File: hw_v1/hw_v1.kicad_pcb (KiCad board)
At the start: 4 copper layers, 116.5 x 98 mm, 230 parts, among them J10 Conn_01x01, J11 Conn_01x01, J12 Delphi_Sicma_24, J13 Delphi_Sicma_24, J14 Conn_01x04, J2 Conn_01x05, J3 Conn_01x05, J4 Conn_01x05, J5 Conn_01x03, J6 Conn_01x04, J8 USB_B, J9 Tag connect, Q1 AO3400A, Q2 AO3400A, Q3 FDS6890A, Q5 SS8050, Q6 AO3400A, SW2 SW_Push, U1 MCZ33810EK, U10 BMP280, U11 L78M05ABDT-TR, U12 LM74800, U13 STM32F407VGTx, U14 TJA1051T-3, U15 25LCxxx, U16 REF3033, U17 SRV05-4, U18 VNLD5090, U19 L78M05ABDT-TR, U2 TC4424A, U21 ADXL343, U3 TC4424A, U4 MAX9926UAEE+, U5 TPL7407LAPWR, U6 LMV324, U7 LMV324, U9 SP720ABTG, Y1 32.768kHz, Y2 25MHz

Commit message: wip sensors pcb layout
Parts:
- added C1: 100nF, Capacitor_SMD:C_0805_2012Metric, F.Cu at (109.5, 73.6)
- added C25: 100nF, Capacitor_SMD:C_0805_2012Metric, F.Cu at (89.5, 73.5)
- added C29: 0.22uF, Capacitor_SMD:C_0603_1608Metric, F.Cu at (91.7, 70.2)
- added C30: 100nF, Capacitor_SMD:C_0805_2012Metric, F.Cu at (76.4, 73.5)
- added C31: 0.01uF, Capacitor_SMD:C_0805_2012Metric, F.Cu at (116.0, 73.4)
- added C46: 0.22uF, Capacitor_SMD:C_0603_1608Metric, F.Cu at (80.3, 73.4)
- added C49: 0.22uF, Capacitor_SMD:C_0603_1608Metric, F.Cu at (113.3, 73.3)
- added C66: 100nF, Capacitor_SMD:C_0805_2012Metric, F.Cu at (83.0, 73.5)
- added C67: 0.22uF, Capacitor_SMD:C_0603_1608Metric, F.Cu at (86.9, 73.4)
- added C68: 100nF, Capacitor_SMD:C_0805_2012Metric, F.Cu at (102.9, 73.7)
- added C69: 0.22uF, Capacitor_SMD:C_0603_1608Metric, F.Cu at (106.7, 73.5)
- added C70: 100nF, Capacitor_SMD:C_0805_2012Metric, F.Cu at (96.3, 73.7)
- added C71: 0.22uF, Capacitor_SMD:C_0603_1608Metric, F.Cu at (100.1, 73.5)
- added Q14: AO3400A, Package_TO_SOT_SMD:SOT-23, F.Cu at (97.4, 82.5)
- added Q15: AO3400A, Package_TO_SOT_SMD:SOT-23, F.Cu at (100.8, 86.4)
- added Q16: AO3400A, Package_TO_SOT_SMD:SOT-23, F.Cu at (93.9, 78.6)
- added Q19: AO3400A, Package_TO_SOT_SMD:SOT-23, F.Cu at (118.9, 73.3)
- added R10: 180k, Resistor_SMD:R_0805_2012Metric, F.Cu at (84.2, 90.2)
- added R13: 180k, Resistor_SMD:R_0805_2012Metric, F.Cu at (78.2, 90.2)
- added R16: 604R, Resistor_SMD:R_0805_2012Metric, F.Cu at (91.6, 73.5)
- added R18: 10k, Resistor_SMD:R_0805_2012Metric, F.Cu at (93.9, 83.4)
- added R28: 3.88k, Resistor_SMD:R_0603_1608Metric, F.Cu at (93.4, 70.2)
- added R44: 348k, Resistor_SMD:R_0805_2012Metric, F.Cu at (78.2, 93.7)
- added R45: 470R, Resistor_SMD:R_0603_1608Metric, F.Cu at (105.9, 71.3)
- added R46: 2.49k +-1%, Resistor_SMD:R_0603_1608Metric, F.Cu at (105.2, 73.5)
- added R47: 180k, Resistor_SMD:R_0805_2012Metric, F.Cu at (76.2, 90.2)
- added R48: 348k, Resistor_SMD:R_0805_2012Metric, F.Cu at (76.2, 93.7)
- added R49: 10k, Resistor_SMD:R_0805_2012Metric, F.Cu at (93.9, 81.3)
- added R50: 10k, Resistor_SMD:R_0805_2012Metric, F.Cu at (93.9, 85.4)
- added R51: 10k, Resistor_SMD:R_0805_2012Metric, F.Cu at (97.8, 79.2)
- added R52: 10k, Resistor_SMD:R_0805_2012Metric, F.Cu at (93.9, 87.4)
- added R53: 10k, Resistor_SMD:R_0805_2012Metric, F.Cu at (97.4, 85.4)
- added R54: 2.49k +-1%, Resistor_SMD:R_0603_1608Metric, F.Cu at (85.3, 73.4)
- added R55: 180k, Resistor_SMD:R_0805_2012Metric, F.Cu at (80.2, 90.2)
- added R56: 470R, Resistor_SMD:R_0603_1608Metric, F.Cu at (93.5, 73.5)
- added R57: 180k, Resistor_SMD:R_0805_2012Metric, F.Cu at (86.2, 90.2)
- added R61: 348k, Resistor_SMD:R_0805_2012Metric, F.Cu at (80.2, 93.7)
- added R62: 180k, Resistor_SMD:R_0805_2012Metric, F.Cu at (88.2, 90.2)
- added R63: 348k, Resistor_SMD:R_0805_2012Metric, F.Cu at (88.2, 93.7)
- added R66: 348k, Resistor_SMD:R_0805_2012Metric, F.Cu at (86.2, 93.7)
- added R67: 180k, Resistor_SMD:R_0805_2012Metric, F.Cu at (82.1, 90.2)
- added R69: 348k, Resistor_SMD:R_0805_2012Metric, F.Cu at (82.1, 93.7)
- added R7: 348k, Resistor_SMD:R_0805_2012Metric, F.Cu at (84.2, 93.7)
- added R74: 2.49k +-1%, Resistor_SMD:R_0603_1608Metric, F.Cu at (78.7, 73.4)
- added R75: 470R, Resistor_SMD:R_0603_1608Metric, F.Cu at (86.1, 71.1)
- added R76: 470R, Resistor_SMD:R_0603_1608Metric, F.Cu at (99.3, 71.3)
- added R77: 470R, Resistor_SMD:R_0603_1608Metric, F.Cu at (79.5, 71.2)
- added R78: 470R, Resistor_SMD:R_0603_1608Metric, F.Cu at (112.6, 70.9)
- added R85: 1k, Resistor_SMD:R_0603_1608Metric, F.Cu at (119.2, 70.5)
- added TP14: TestPoint_Alt, TestPoint:TestPoint_THTPad_1.0x1.0mm_Drill0.5mm, F.Cu at (83.0, 70.7)
- added TP15: TestPoint_Alt, TestPoint:TestPoint_THTPad_1.0x1.0mm_Drill0.5mm, F.Cu at (102.8, 70.9)
- added TP19: TestPoint_Alt, TestPoint:TestPoint_THTPad_1.0x1.0mm_Drill0.5mm, F.Cu at (96.3, 70.9)
- added TP20: TestPoint_Alt, TestPoint:TestPoint_THTPad_1.0x1.0mm_Drill0.5mm, F.Cu at (89.7, 70.6)
- added TP23: TestPoint_Alt, TestPoint:TestPoint_THTPad_1.0x1.0mm_Drill0.5mm, F.Cu at (76.4, 70.7)
- added TP25: TestPoint_Alt, TestPoint:TestPoint_THTPad_1.0x1.0mm_Drill0.5mm, F.Cu at (109.5, 70.6)
- added TP38: TestPoint_Alt, TestPoint:TestPoint_THTPad_1.0x1.0mm_Drill0.5mm, F.Cu at (116.0, 70.6)
- added U10: LMV324, Package_SO:TSSOP-14_4.4x5mm_P0.65mm, F.Cu at (103.1, 91.9)
- added U2: 74HC4851, Package_SO:SOIC-16_3.9x9.9mm_P1.27mm, F.Cu at (88.0, 83.2)
- added U26: SP720ABTG, Package_SO:SOP-16_3.9x9.9mm_P1.27mm, F.Cu at (79.0, 83.2)
- added U9: LMV324, Package_SO:TSSOP-14_4.4x5mm_P0.65mm, F.Cu at (94.2, 91.9)
- moved D3 194.3 mm to (64.4, 110.6), turned to 90 degrees
- moved D6 192.0 mm to (66.5, 110.6), turned to 90 degrees
- moved TP15 189.8 mm to (22.1, 51.0), turned to 90 degrees
- moved D8 189.7 mm to (68.6, 110.6), turned to 90 degrees
- moved TP16 188.1 mm to (25.1, 51.0), turned to 90 degrees
- moved D11 187.4 mm to (70.7, 110.6), turned to 90 degrees
- moved TP11 185.9 mm to (22.1, 54.0), turned to 90 degrees
- moved TP14 184.1 mm to (25.1, 54.0), turned to 90 degrees
- moved TP9 182.0 mm to (22.1, 57.1), turned to 90 degrees
- moved RN1 181.5 mm to (67.5, 101.2), turned to -90 degrees
- moved D12 180.9 mm to (64.4, 97.4), turned to -90 degrees
- moved D2 180.7 mm to (64.3, 106.7), turned to 90 degrees
- moved TP10 180.2 mm to (25.1, 57.1), turned to 90 degrees
- moved RN2 179.1 mm to (74.0, 106.6), turned to -90 degrees
- moved D9 178.3 mm to (66.5, 97.4), turned to -90 degrees
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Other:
- board text added: "1"
- board text added: "ACC"
- board text added: "Analog frontend"
- board text added: "CLT"
- board text added: "EXT O2"
- board text added: "IAT"
- board text added: "Ignicion"
- board text added: "Inyeccion"
- board text added: "MAP"
- board text added: "TPS"
- board text added: "VBAT"

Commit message: wip sensors pcb layout
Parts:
- removed the C1 at (200.2, 55.3)
- removed the C1 at (109.5, 73.6)
- removed the C25 at (234.9, 137.5)
- removed the C25 at (89.5, 73.5)
- removed the C29 at (91.7, 70.2)
- removed the C29 at (173.3, 58.3)
- removed the C30 at (173.3, 61.3)
- removed the C30 at (76.4, 73.5)
- removed the C31 at (173.3, 64.3)
- removed the C31 at (116.0, 73.4)
- removed the C46 at (80.3, 73.4)
- removed the C46 at (188.3, 95.8)
- removed the C49 at (113.3, 73.3)
- removed C66, C68, C70: 100nF, Capacitor_SMD:C_0805_2012Metric
- removed C67, C69, C71: 0.22uF, Capacitor_SMD:C_0603_1608Metric
- removed Q14, Q15, Q16, Q19: AO3400A, Package_TO_SOT_SMD:SOT-23
- removed the R10 at (84.2, 90.2)
- removed the R10 at (215.0, 75.1)
- removed the R13 at (78.2, 90.2)
- removed the R13 at (234.9, 122.1)
- removed the R16 at (234.9, 125.1)
- removed the R16 at (91.6, 73.5)
- removed the R18 at (33.0, 65.8)
- removed the R18 at (93.9, 83.4)
- removed the R28 at (30.5, 61.8)
- removed the R28 at (93.4, 70.2)
- removed the R44 at (180.8, 100.2)
- removed the R44 at (78.2, 93.7)
- removed the R45 at (31.8, 98.8)
- removed the R45 at (105.9, 71.3)
- removed the R46 at (17.1, 94.4)
- removed the R46 at (105.2, 73.5)
- removed the R47 at (76.2, 90.2)
- removed the R47 at (20.0, 94.4)
- removed the R48 at (76.2, 93.7)
- removed the R48 at (228.2, 101.4)
- removed the R49 at (93.9, 81.3)
- removed the R49 at (228.2, 103.9)
- removed the R50 at (22.9, 94.4)
- removed the R50 at (93.9, 85.4)
- removed the R51 at (25.9, 94.4)
- removed the R51 at (97.8, 79.2)
- removed the R52 at (28.9, 94.4)
- removed the R52 at (93.9, 87.4)
- removed the R53 at (97.4, 85.4)
- removed the R53 at (246.6, 134.5)
- removed the R54 at (246.6, 137.0)
- removed the R54 at (85.3, 73.4)
- removed the R55 at (80.2, 90.2)
- removed the R55 at (251.7, 125.8)
- removed the R56 at (93.5, 73.5)
- removed the R56 at (251.7, 128.7)
- removed the R57 at (251.7, 131.7)
- removed the R57 at (86.2, 90.2)
- removed the R61 at (228.2, 111.4)
- removed the R61 at (80.2, 93.7)
- removed the R62 at (88.2, 90.2)
- removed the R63 at (88.2, 93.7)
- removed the R66 at (86.2, 93.7)
- removed the R67 at (82.1, 90.2)
- removed R69: 348k, Resistor_SMD:R_0805_2012Metric
- removed the R7 at (84.2, 93.7)
- removed the R7 at (195.2, 72.7)
- removed R74: 2.49k +-1%, Resistor_SMD:R_0603_1608Metric
- removed R75, R76, R77, R78: 470R, Resistor_SMD:R_0603_1608Metric
- removed R85: 1k, Resistor_SMD:R_0603_1608Metric
- removed the TP14 at (25.1, 54.0)
- removed the TP14 at (83.0, 70.7)
- removed the TP15 at (22.1, 51.0)
- removed the TP15 at (102.8, 70.9)
- removed TP19, TP20, TP23, TP25, TP38: TestPoint_Alt, TestPoint:TestPoint_THTPad_1.0x1.0mm_Drill0.5mm
- removed the U10 at (125.7, 102.5)
- removed the U10 at (103.1, 91.9)
- removed the U2 at (88.0, 83.2)
- removed U26: SP720ABTG, Package_SO:SOP-16_3.9x9.9mm_P1.27mm
- removed the U9 at (94.2, 91.9)
- removed the U9 at (22.3, 86.5)
- added C1: 0.01uF, Capacitor_SMD:C_0805_2012Metric, F.Cu at (222.3, 60.6)
- added C25: 0.1uF, Capacitor_SMD:C_0805_2012Metric, F.Cu at (240.4, 110.0)
- added C29: 2.2uF, Capacitor_SMD:C_0805_2012Metric, F.Cu at (192.0, 63.7)
- added C30: 100nF, Capacitor_SMD:C_0805_2012Metric, F.Cu at (192.0, 66.7)
- added C31: 100nF, Capacitor_SMD:C_0805_2012Metric, F.Cu at (192.0, 69.7)
- added C46: 100n, Capacitor_SMD:C_0402_1005Metric, F.Cu at (207.9, 76.1)
- added R10: 10k, Resistor_SMD:R_0603_1608Metric, F.Cu at (226.6, 79.6)
- added R13: 470R, Resistor_SMD:R_0805_2012Metric, F.Cu at (102.1, 70.6)
- added R16: 1k, Resistor_SMD:R_0805_2012Metric, F.Cu at (240.3, 97.6)
- added R18: 470R, Resistor_SMD:R_0603_1608Metric, F.Cu at (95.6, 71.1)
- added R28: 470R, Resistor_SMD:R_0603_1608Metric, F.Cu at (95.6, 78.9)
- added R44: 4.7k, Resistor_SMD:R_0603_1608Metric, F.Cu at (187.8, 78.0)
- added R45: 180k, Resistor_SMD:R_0805_2012Metric, F.Cu at (192.4, 97.6)
- added R46: 180k, Resistor_SMD:R_0805_2012Metric, F.Cu at (191.6, 100.4)
- added R47: 180k, Resistor_SMD:R_0805_2012Metric, F.Cu at (196.8, 91.7)
- added R48: 1k, Resistor_SMD:R_0603_1608Metric, F.Cu at (211.1, 117.8)
- added R49: 1k, Resistor_SMD:R_0603_1608Metric, F.Cu at (211.1, 120.3)
- added R50: 348k, Resistor_SMD:R_0805_2012Metric, F.Cu at (196.8, 94.7)
- added R51: 348k, Resistor_SMD:R_0805_2012Metric, F.Cu at (196.8, 97.6)
- added R52: 348k, Resistor_SMD:R_0805_2012Metric, F.Cu at (196.8, 100.6)
- added R53: 1k, Resistor_SMD:R_0603_1608Metric, F.Cu at (227.0, 130.9)
- added R54: 100k, Resistor_SMD:R_0603_1608Metric, F.Cu at (227.0, 133.4)
- added R55: 100k, Resistor_SMD:R_0805_2012Metric, F.Cu at (232.1, 122.2)
- added R56: 100k, Resistor_SMD:R_0805_2012Metric, F.Cu at (232.1, 125.2)
- added R57: 1k, Resistor_SMD:R_0805_2012Metric, F.Cu at (232.1, 128.2)
- added R61: 1k, Resistor_SMD:R_0603_1608Metric, F.Cu at (211.1, 127.8)
- added R7: 4.99K 1/2W, Resistor_SMD:R_1210_3225Metric, F.Cu at (217.3, 78.1)
- added TP14: TestPoint_Alt, TestPoint:TestPoint_THTPad_1.0x1.0mm_Drill0.5mm, F.Cu at (79.3, 78.5)
- added TP15: TestPoint_Alt, TestPoint:TestPoint_THTPad_1.0x1.0mm_Drill0.5mm, F.Cu at (86.0, 78.5)
- added TP17: TestPoint_Alt, TestPoint:TestPoint_THTPad_1.0x1.0mm_Drill0.5mm, F.Cu at (99.2, 78.6)
- added TP18: TestPoint_Alt, TestPoint:TestPoint_THTPad_1.0x1.0mm_Drill0.5mm, F.Cu at (99.2, 70.6)
- added U10: BMP280, Package_LGA:Bosch_LGA-8_2x2.5mm_P0.65mm_ClockwisePinNumbering, F.Cu at (200.7, 103.9)
- added U9: SP720ABTG, Package_SO:SOP-16_3.9x9.9mm_P1.27mm, F.Cu at (194.4, 107.8)
- moved R35 171.0 mm to (188.0, 94.7), turned to 0 degrees
- moved R36 168.0 mm to (188.0, 97.6), turned to 0 degrees
- moved R17 166.9 mm to (183.5, 91.7), turned to 0 degrees
- moved R40 166.6 mm to (192.4, 91.7), turned to 0 degrees
- moved R39 165.0 mm to (188.0, 100.6), turned to 0 degrees
- moved R23 160.8 mm to (183.5, 94.7), turned to 0 degrees
- moved R24 157.7 mm to (183.5, 97.6), turned to 0 degrees
- moved R33 156.6 mm to (188.0, 91.7), turned to 0 degrees
- moved R26 154.7 mm to (183.5, 100.6), turned to 0 degrees
- moved U6 150.0 mm to (185.7, 105.3), turned to 0 degrees
- moved C20 148.8 mm to (99.2, 73.5), turned to -90 degrees
- moved R41 147.4 mm to (176.0, 90.8), turned to 0 degrees
- moved C19 144.6 mm to (99.2, 81.5), turned to -90 degrees
- moved U7 144.4 mm to (185.7, 111.9), turned to 0 degrees
- moved R12 138.8 mm to (102.1, 78.6), turned to 180 degrees
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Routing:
- net /Sensors/CH_VBATT_m: track 0.00 -> 9.14 mm, vias 0 -> 1
- net Net-(C23-Pad1): track 0.00 -> 6.29 mm
- net /Sensors/CH_O2_m: track 0.00 -> 6.07 mm
- net /Sensors/CH_MAP_m: track 0.00 -> 5.92 mm
- net /Protoboard/ext_a0_in: track 0.00 -> 5.91 mm
- net /Sensors/CH_TPS_m: track 0.00 -> 5.89 mm
- net /Sensors/CH_CLT_m: track 0.00 -> 5.89 mm
- net /Sensors/CH_IAT_m: track 0.00 -> 5.86 mm
- net /Protoboard/ext_a1_in: track 0.00 -> 5.80 mm
- net O2_Sensor: track 0.00 -> 5.69 mm
- net TPS_Sensor: track 0.00 -> 5.32 mm
- net CH_MAP: track 0.00 -> 4.63 mm
- net IAT_Sensor: track 0.00 -> 4.62 mm
- net CLT_Sensor: track 0.00 -> 4.56 mm
- net Net-(D5-K): track 0.00 -> 3.72 mm
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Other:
- board text added: "AUX_IN0"
- board text added: "AUX_IN1"
- board text added: "Inyección"
- board text removed: "ACC"
- board text removed: "Analog frontend"
- board text removed: "Inyeccion"

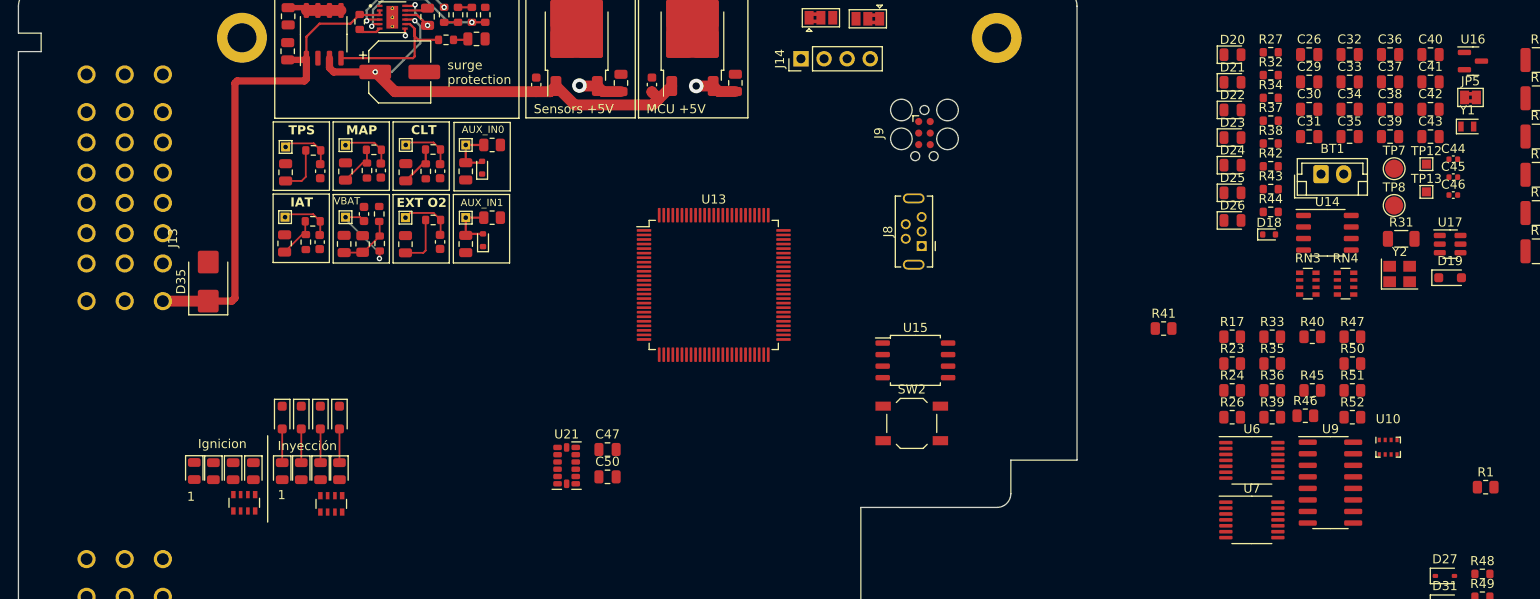
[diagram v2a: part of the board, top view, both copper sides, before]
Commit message: wip sensors traces, added can
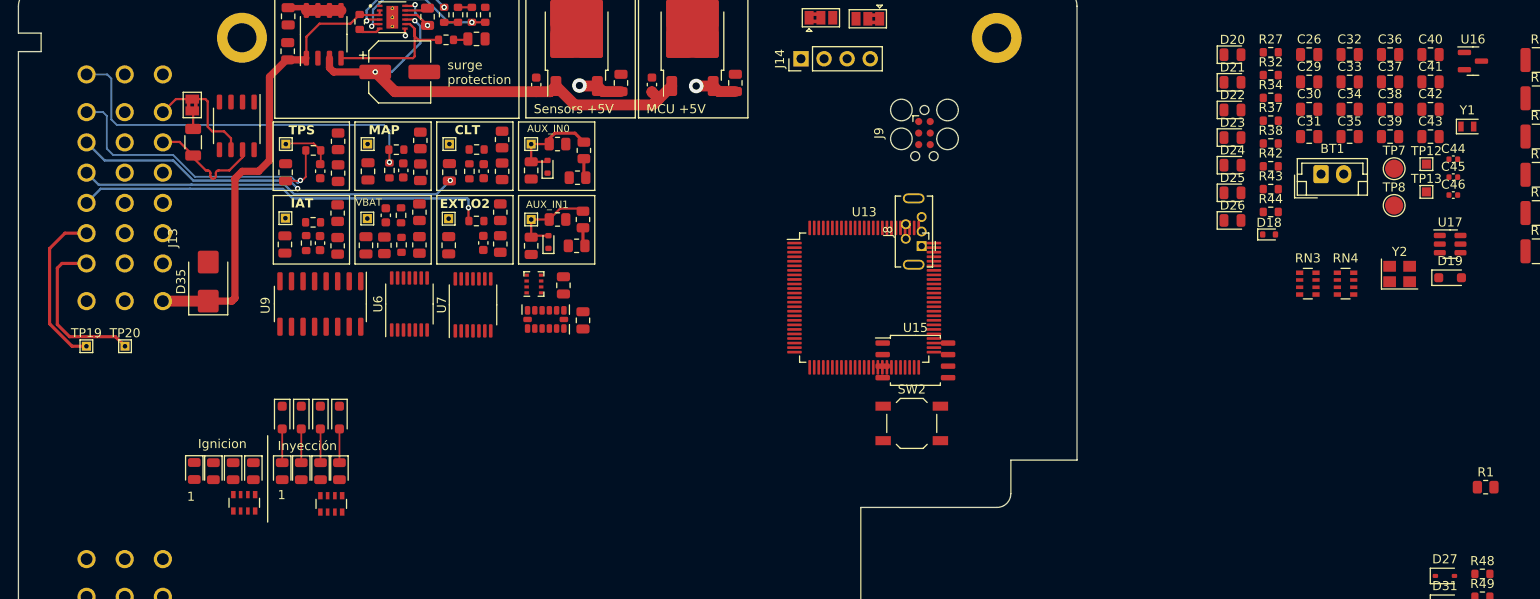
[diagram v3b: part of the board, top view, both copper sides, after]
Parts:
- added TP19: TestPoint_Alt, TestPoint:TestPoint_THTPad_1.0x1.0mm_Drill0.5mm, F.Cu at (57.5, 92.8)
- added TP20: TestPoint_Alt, TestPoint:TestPoint_THTPad_1.0x1.0mm_Drill0.5mm, F.Cu at (61.7, 92.8)
- moved JP5 140.7 mm to (69.1, 66.2), turned to -90 degrees
- moved R31 133.4 mm to (69.2, 70.3), turned to -90 degrees
- moved U14 120.6 mm to (74.0, 68.5), turned to -90 degrees
- moved R51 114.9 mm to (85.2, 70.2), turned to 90 degrees
- moved U9 112.9 mm to (83.2, 88.1), turned to -90 degrees
- moved R46 109.7 mm to (85.2, 73.7), turned to -90 degrees
- moved R39 105.3 mm to (85.1, 78.1), turned to 90 degrees
- moved R33 103.3 mm to (85.1, 81.7), turned to 90 degrees
- moved R40 99.2 mm to (94.1, 78.0), turned to 90 degrees
- moved R36 96.8 mm to (94.2, 73.6), turned to -90 degrees
- moved R50 96.8 mm to (103.2, 70.0), turned to 90 degrees
- moved R52 96.5 mm to (103.0, 78.0), turned to 90 degrees
- moved U10 95.7 mm to (106.7, 85.9), turned to 90 degrees
- moved R35 94.8 mm to (94.1, 81.6), turned to -90 degrees
- moved R47 94.3 mm to (103.0, 81.5), turned to -90 degrees
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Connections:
- net CAM-IN+ renamed CRANK-
- net CRANK-IN+ renamed CAM-
- net CRANK-IN- renamed CRANK+
- net IGN1 renamed STEPPER-B2
- net IGN2 renamed STEPPER-B1
- net IGN4 renamed STEPPER-A2
- C13 pad 1: CH_MAP -> MAP_Sensor
- C19 pad 1: /Protoboard/ext_a0_in -> ext_a0_in
- C20 pad 1: /Protoboard/ext_a1_in -> ext_a1_in
- D16 pad 2: /Protoboard/ext_a0_in -> ext_a0_in
- D17 pad 2: /Protoboard/ext_a1_in -> ext_a1_in
- J12 pad A1: INJ1 -> INJ-1-OUT
- J12 pad A2: INJ2 -> INJ-2-OUT
- J12 pad A3: INJ3 -> INJ-3-OUT
- J12 pad A4: INJ4 -> INJ-4-OUT
- J12 pad A5: INJ5 -> IGN-1-OUT
- J12 pad A6: INJ6 -> IGN-2-OUT
- J12 pad A7: INJ7 -> IGN-3-OUT
- J12 pad A8: INJ8 -> IGN-4-OUT
- J12 pad B3: IGN3 -> STEPPER-A1
- J12 pad B5: IGN5 -> FAN-OUT
- J12 pad B6: IGN6 -> FAN2-OUT
- J12 pad B7: IGN7 -> FUELPUMP-OUT
- J12 pad B8: IGN8 -> TACHO-OUT
- J12 pad C2: FAN-OUT -> VVT-OUT
- J12 pad C3: SPARE2-OUT -> IDLE-OUT
- J12 pad C4: IDLE-OUT -> PROTO-4
- J12 pad C5: STEPPER-A1 -> PROTO-3
- J12 pad C6: SPARE1-OUT -> PROTO-2
- J12 pad C7: FUELPUMP-OUT -> PROTO-1
- J13 pad A4: unconnected-(J13-PadA4) -> PROTO-5
- J13 pad A5: SPARE2-Digital -> Clutch_in
- J13 pad A6: CAN_L -> CAN+
- J13 pad A7: CAN_H -> CAN-
- J13 pad B1: TACHO-OUT -> CAM+
- J13 pad B5: CAM-IN- -> SW_USER
- J13 pad B6: SPARE1-Digital -> SW_TABLE
- J13 pad B7: Clutch_in -> SW_SHIFT
- J13 pad B8: Flex_Sensor -> SW_AC
- J13 pad C1: GND -> GNDREF
- R12 pad 2: /Protoboard/ext_a0_in -> ext_a0_in
- R13 pad 1: /Protoboard/ext_a1_in -> ext_a1_in
- R15 pad 1: CH_MAP -> MAP_Sensor
- R17 pad 2: /Sensors/ext_a1_in -> ext_a1_in
- R20 pad 2: CH_MAP -> MAP_Sensor
- R24 pad 2: /Sensors/ext_a0_in -> ext_a0_in
- TP17 pad 1: /Protoboard/ext_a0_in -> ext_a0_in
- TP18 pad 1: /Protoboard/ext_a1_in -> ext_a1_in
- U5 pad 12: STEPPER-A1 -> VVT-OUT
- U5 pad 13: STEPPER-A1 -> VVT-OUT
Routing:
- net MAP_Sensor: track 0.00 -> 43.4 mm, vias 0 -> 1
- net O2_Sensor: track 5.69 -> 45.6 mm, vias 0 -> 1
- net CLT_Sensor: track 4.56 -> 41.6 mm, vias 0 -> 1
- net TPS_Sensor: track 5.32 -> 34.4 mm, vias 0 -> 1
- net IAT_Sensor: track 4.62 -> 25.3 mm, vias 0 -> 1
- net SPARE2_Sensor: track 0.00 -> 18.1 mm
- net SPARE1_Sensor: track 0.00 -> 18.1 mm
- net CAN+: track 0.00 -> 12.9 mm
- net CAN-: track 0.00 -> 12.8 mm
- net ext_a1_in: track 0.00 -> 10.9 mm
- net ext_a0_in: track 0.00 -> 10.2 mm
- net /Sensors/CH_VBATT_m: track 9.14 -> 0.00 mm, vias 1 -> 0
- net Net-(C23-Pad1): track 6.29 -> 0.09 mm
- net /Sensors/CH_O2_m: track 6.07 -> 0.00 mm
- net /Sensors/CH_MAP_m: track 5.92 -> 0.00 mm
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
